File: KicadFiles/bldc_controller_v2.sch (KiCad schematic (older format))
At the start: 175 parts, among them J1 Conn_01x05_Male, J10 Conn_01x02_Female, J11 Conn_01x02_Female, J12 Conn_01x02_Female, J13 Conn_01x02_Female, J14 Conn_01x02_Female, J15 Conn_01x04_Male, J2 Conn_01x03_Male, J3 Conn_01x03_Male, J4 1935174, J5 Conn_01x02_Female, J9 Conn_01x02_Female, Q10 IRLB8721PBF, Q11 IRLB8721PBF, Q2 DMN65D8L-7, Q3 DMN65D8L-7, Q5 IRF4905, Q6 IRLB8721PBF, Q7 IRLB8721PBF, Q8 IRLB8721PBF, Q9 IRLB8721PBF, SW2 D6C40 F1 LFS, SW3 1301.9314, SW4 1301.9314, SW5 SW_Push_DPDT, U1 ATmega328P-PU, U2 uA7810, U3 LM7805_TO220, U4 MCP601-xP, U5 LM339, U6 IRS2004, U7 IRS2004, U8 IRS2004, U9 HCPL-181-00DE, Y1 9B-16.000MBBK-B

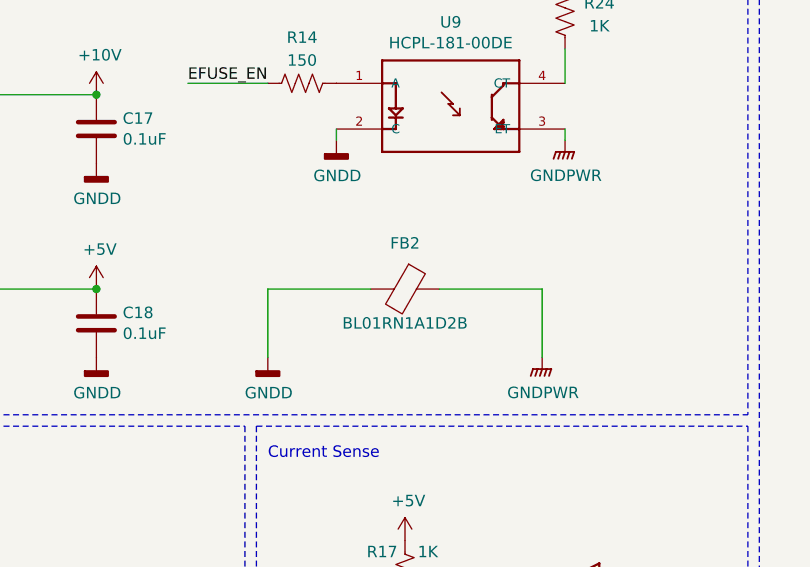
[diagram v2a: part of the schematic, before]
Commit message: Replaced FB with Jumper
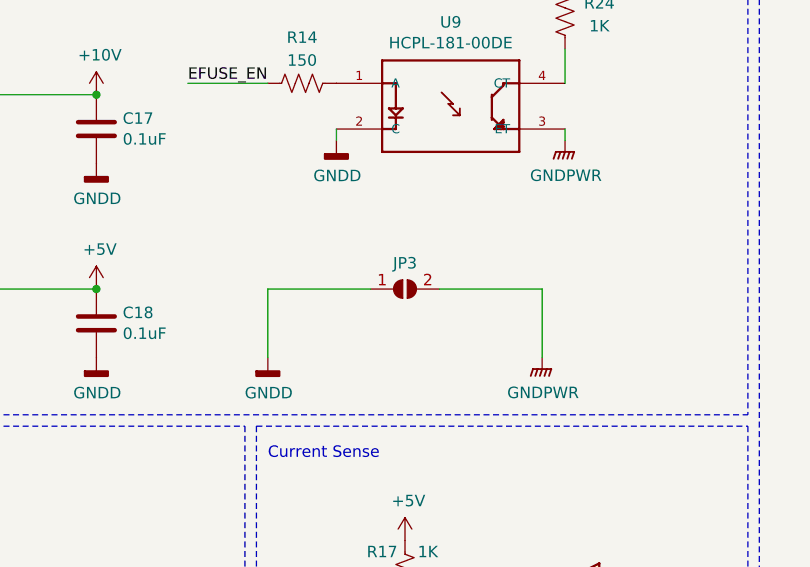
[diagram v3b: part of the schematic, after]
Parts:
- removed FB2: BL01RN1A1D2B, Ferrite_THT:Ferrite_Bead_TH, symbol Device:Ferrite_Bead
- added JP3: SolderJumper_2_Open, Jumper:Solder_Jumper_2_Pin_5A, symbol Jumper:SolderJumper_2_Open
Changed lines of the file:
@@
 Wire Wire Line
 	5500 1900 6000 1900
-$Comp
-L Device:Ferrite_Bead FB2
-U 1 1 5E13E3A5
-P 8400 2750
-F 0 "FB2" V 8200 2750 50  0000 C CNN
-F 1 "BL01RN1A1D2B" V 8550 2750 50  0000 C CNN
-F 2 "Ferrite_THT:Ferrite_Bead_TH" V 8330 2750 50  0001 C CNN
-F 3 "~" H 8400 2750 50  0001 C CNN
-	1    8400 2750
-	0    1    1    0
-$EndComp
 Wire Wire Line
 	8550 2750 9000 2750
@@
 Wire Wire Line
 	2400 1950 2400 2150
+$Comp
+L Jumper:SolderJumper_2_Open JP3
+U 1 1 5EB572A6
+P 8400 2750
+F 0 "JP3" H 8400 2863 50  0000 C CNN
+F 1 "SolderJumper_2_Open" H 8400 2864 50  0001 C CNN
+F 2 "Jumper:Solder_Jumper_2_Pin_5A" H 8400 2750 50  0001 C CNN
+F 3 "~" H 8400 2750 50  0001 C CNN
+	1    8400 2750
+	1    0    0    -1
+$EndComp
 $EndSCHEMATC

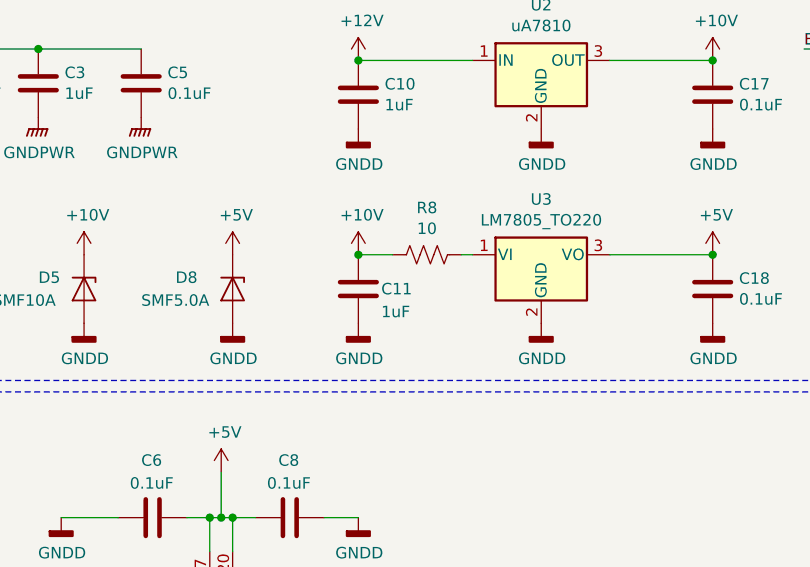
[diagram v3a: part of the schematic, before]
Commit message: Updated 5V Regulator
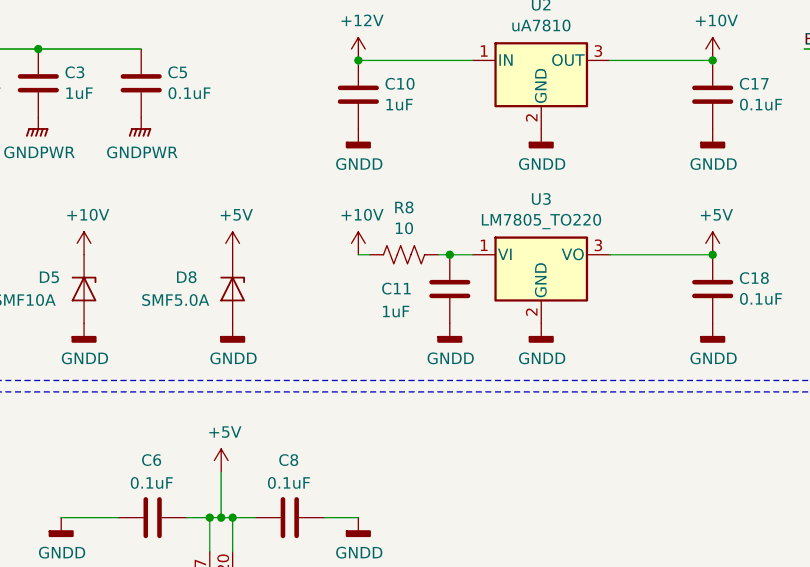
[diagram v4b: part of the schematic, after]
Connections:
- wire segments 325 -> 326
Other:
- moved on the sheet: C11, R8
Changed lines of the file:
@@
 $EndComp
 Wire Wire Line
-	5950 2750 6000 2750
+	5850 2750 5900 2750
 Wire Wire Line
-	5650 2750 5500 2750
+	5550 2750 5500 2750
 $Comp
 L Device:R_US R8
 U 1 1 5DF60A47
-P 5800 2750
-F 0 "R8" V 5595 2750 50  0000 C CNN
-F 1 "10" V 5686 2750 50  0000 C CNN
-F 2 "Resistor_SMD:R_0805_2012Metric_Pad1.15x1.40mm_HandSolder" V 5840 2740 50  0001 C CNN
-F 3 "~" H 5800 2750 50  0001 C CNN
-	1    5800 2750
+P 5700 2750
+F 0 "R8" V 5495 2750 50  0000 C CNN
+F 1 "10" V 5586 2750 50  0000 C CNN
+F 2 "Resistor_SMD:R_0805_2012Metric_Pad1.15x1.40mm_HandSolder" V 5740 2740 50  0001 C CNN
+F 3 "~" H 5700 2750 50  0001 C CNN
+	1    5700 2750
 	0    1    1    0
 $EndComp
@@
 L power:GNDD #PWR052
 U 1 1 5DC455A1
-P 5500 3050
-F 0 "#PWR052" H 5500 2800 50  0001 C CNN
-F 1 "GNDD" H 5504 2895 50  0000 C CNN
-F 2 "" H 5500 3050 50  0001 C CNN
-F 3 "" H 5500 3050 50  0001 C CNN
-	1    5500 3050
+P 5900 3050
+F 0 "#PWR052" H 5900 2800 50  0001 C CNN
+F 1 "GNDD" H 5904 2895 50  0000 C CNN
+F 2 "" H 5900 3050 50  0001 C CNN
+F 3 "" H 5900 3050 50  0001 C CNN
+	1    5900 3050
 	1    0    0    -1
 $EndComp
@@
 $EndComp
 Connection ~ 5500 1900
-Connection ~ 5500 2750
 $Comp
 L power:+5V #PWR013
@@
 L Device:C C11
 U 1 1 5FB5131F
-P 5500 2900
+P 5900 2900
 F 0 "C11" H 5600 2900 50  0000 L CNN
 F 1 "1uF" H 5600 2800 50  0000 L CNN
-F 2 "Capacitor_SMD:C_0805_2012Metric_Pad1.15x1.40mm_HandSolder" H 5538 2750 50  0001 C CNN
-F 3 "~" H 5500 2900 50  0001 C CNN
-	1    5500 2900
+F 2 "Capacitor_SMD:C_0805_2012Metric_Pad1.15x1.40mm_HandSolder" H 5938 2750 50  0001 C CNN
+F 3 "~" H 5900 2900 50  0001 C CNN
+	1    5900 2900
 	1    0    0    -1
 $EndComp
@@
 	1    0    0    -1
 $EndComp
+Connection ~ 5900 2750
+Wire Wire Line
+	5900 2750 6000 2750
 $EndSCHEMATC

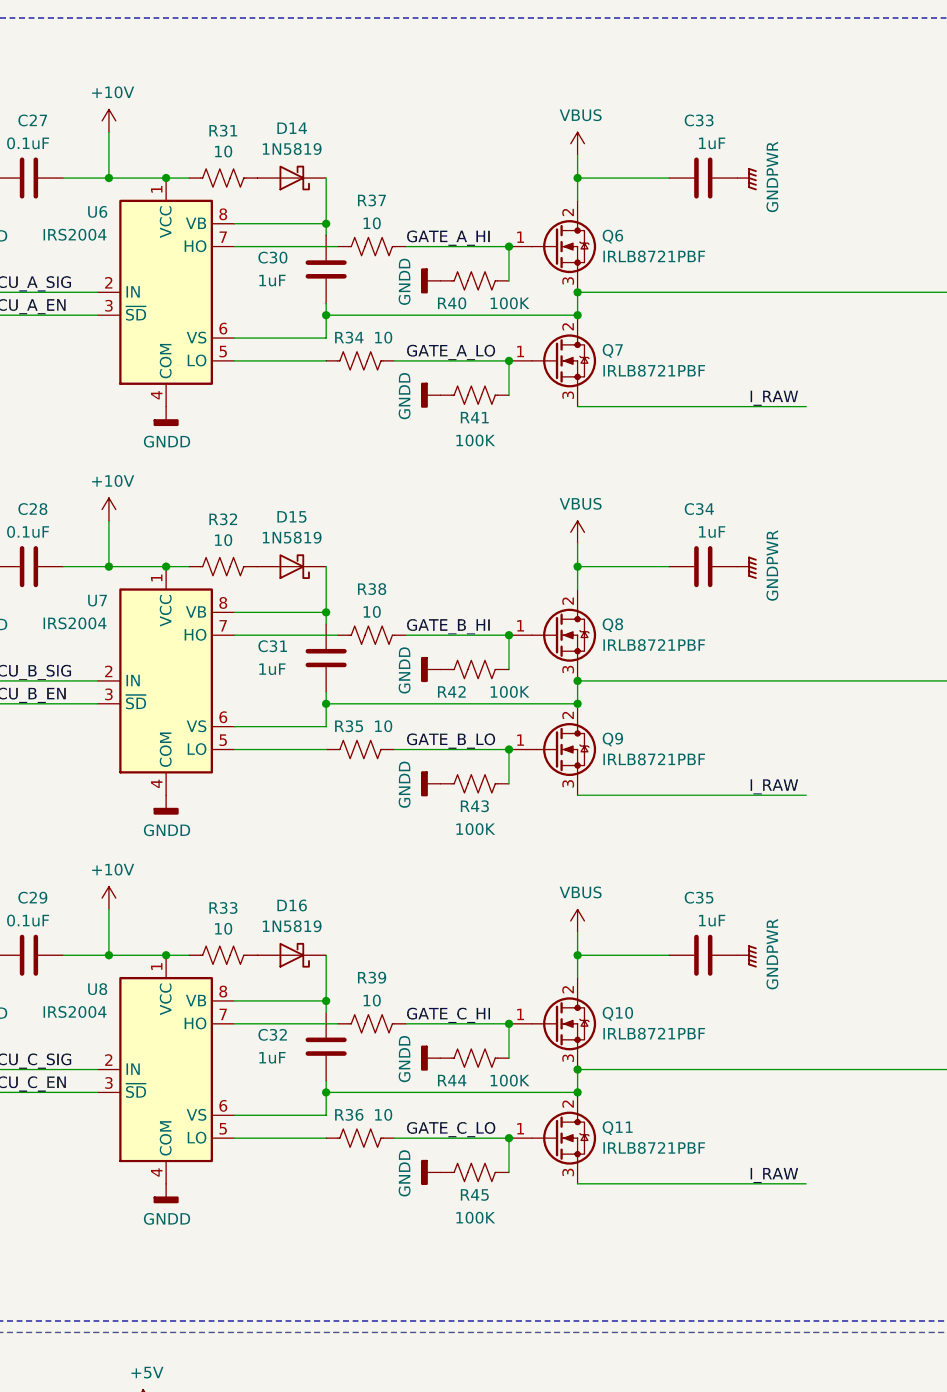
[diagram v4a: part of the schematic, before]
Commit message: Updated FET Placement
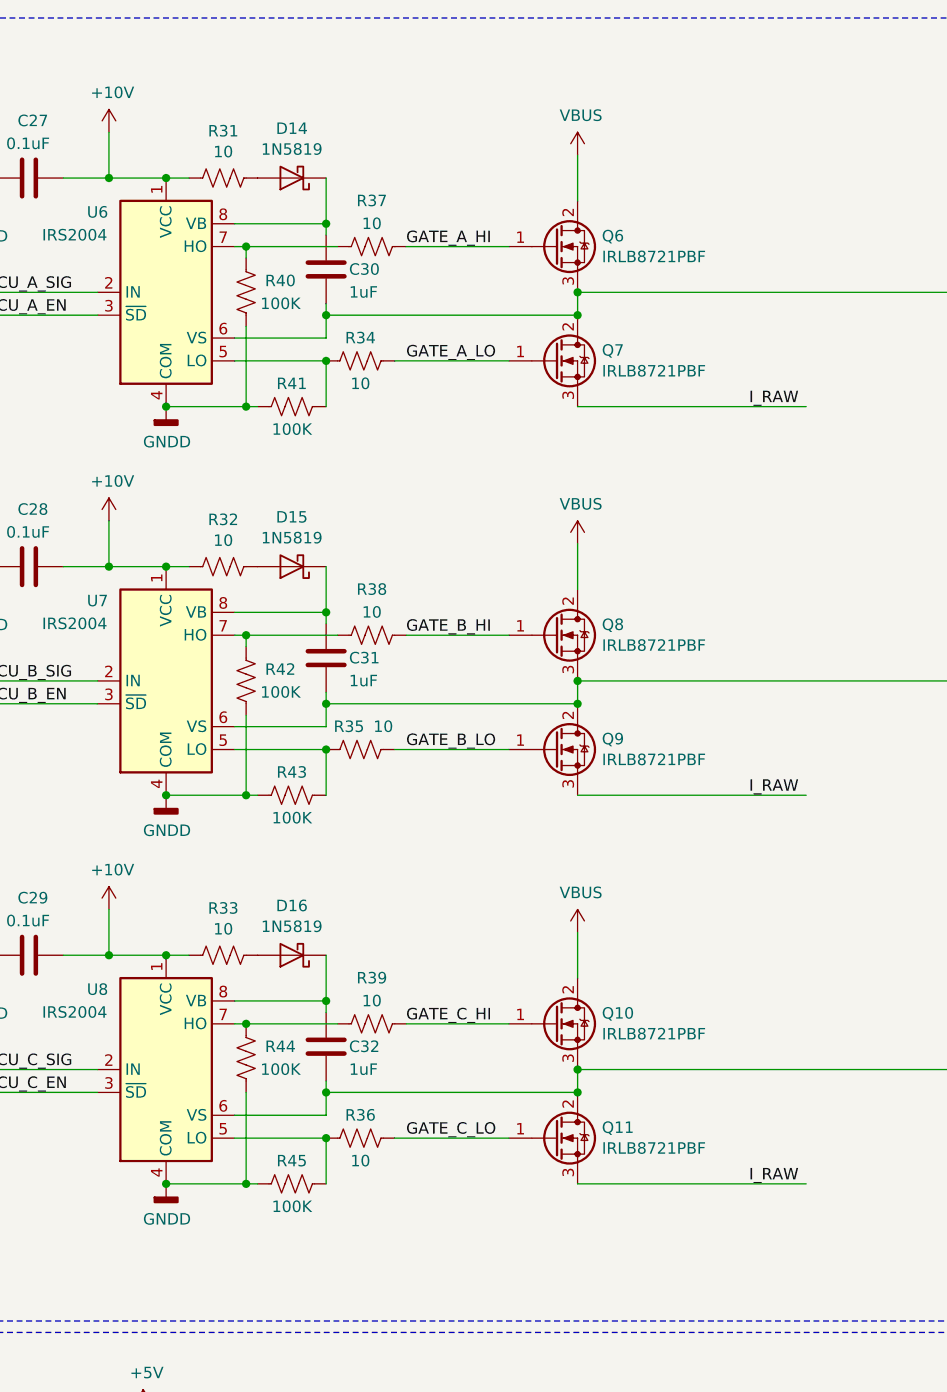
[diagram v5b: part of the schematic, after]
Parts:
- removed C33, C34, C35: 1uF, Capacitor_SMD:C_0805_2012Metric_Pad1.15x1.40mm_HandSolder, symbol Device:C
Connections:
- wire segments 326 -> 331
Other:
- moved on the sheet: R40, R41, R42, R43, R44, R45

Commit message: Ready to Route
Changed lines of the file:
@@
 Text Label 1800 1750 0    50   ~ 0
 EXT_nRST
-Text Label 1800 2050 0    50   ~ 0
-TXD
-Text Label 1800 2150 0    50   ~ 0
-RXD
 $Comp
 L power:+12V #PWR023
@@
 $EndComp
 Wire Wire Line
-	2400 1850 2400 1700
-Wire Wire Line
 	1750 1750 2200 1750
 Wire Wire Line
@@
 Connection ~ 12350 8400
 Wire Wire Line
-	1750 2150 2200 2150
-Wire Wire Line
-	1750 2050 2200 2050
-Wire Wire Line
-	1750 1850 2400 1850
-Wire Wire Line
-	1750 1950 2400 1950
-Wire Wire Line
 	1750 2750 2150 2750
 Text Label 1750 2750 0    50   ~ 0
@@
 Wire Wire Line
 	5450 4650 6050 4650
-Text Label 5600 6250 0    50   ~ 0
+Text Label 5600 6350 0    50   ~ 0
 nI_TRIG
-Text Label 5600 6450 0    50   ~ 0
+Text Label 5600 4750 0    50   ~ 0
 AUX_OUT
-Text Label 5600 5350 0    50   ~ 0
+Text Label 5600 4650 0    50   ~ 0
 EFUSE_EN
 Text Label 5600 5850 0    50   ~ 0
 nRESET
-Text Label 5600 6550 0    50   ~ 0
+Text Label 5600 4850 0    50   ~ 0
 nESTOP
-Text Label 5600 5550 0    50   ~ 0
-I_SENSE
 Text Label 5600 5450 0    50   ~ 0
-ANALOG_IN
-Text Label 5600 5250 0    50   ~ 0
+I_SENSE
+Text Label 5600 4350 0    50   ~ 0
 MCU_A_EN
-Text Label 5600 4850 0    50   ~ 0
+Text Label 5600 6750 0    50   ~ 0
 MCU_B_EN
-Text Label 5600 4750 0    50   ~ 0
+Text Label 5600 6550 0    50   ~ 0
 MCU_C_EN
-Text Label 5600 4650 0    50   ~ 0
+Text Label 5600 4450 0    50   ~ 0
 MCU_A_SIG
 Text Label 5600 4550 0    50   ~ 0
 MCU_B_SIG
-Text Label 5600 4450 0    50   ~ 0
+Text Label 5600 6650 0    50   ~ 0
 MCU_C_SIG
-Text Label 5600 4350 0    50   ~ 0
+Text Label 5600 6450 0    50   ~ 0
 BEMF_B
-Text Label 5600 6650 0    50   ~ 0
+Text Label 5600 5550 0    50   ~ 0
 BEMF_A
-Text Label 5600 6750 0    50   ~ 0
+Text Label 5600 6250 0    50   ~ 0
 BEMF_C
-Text Label 5600 6350 0    50   ~ 0
+Text Label 5600 5350 0    50   ~ 0
 AUX_IN
 Wire Wire Line
@@
 	1    0    0    -1
 $EndComp
-Wire Wire Line
-	2400 1950 2400 2150
 $Comp
 L Jumper:SolderJumper_2_Open JP3
@@
 	11850 5700 11850 5500
 Connection ~ 11850 5500
+Wire Wire Line
+	1750 2050 2200 2050
+Wire Wire Line
+	1750 2150 2200 2150
+Wire Wire Line
+	2400 1850 2400 1700
+Wire Wire Line
+	2400 1950 2400 2150
+Text Label 1800 2150 0    50   ~ 0
+RXD
+Text Label 1800 2050 0    50   ~ 0
+TXD
+Wire Wire Line
+	1750 1950 2400 1950
+Wire Wire Line
+	1750 1850 2400 1850
+Text Label 5600 5250 0    50   ~ 0
+ANALOG_IN
 $EndSCHEMATC

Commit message: Finished Planes
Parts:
- J10, J11, J12, J13, J14, J5, J9: footprint Connector_PinHeader_2.54mm:PinHeader_1x02_P2.54mm_Vertical -> Connector_PinSocket_2.54mm:PinSocket_1x02_P2.54mm_Vertical
- TP18, TP2, TP34, TP4: footprint TestPoint:TestPoint_THTPad_1.0x1.0mm_Drill0.5mm -> TestPoint:TestPoint_Keystone_5000-5004_Miniature
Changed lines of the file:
@@
 F 0 "J14" H 13150 6800 50  0000 C CNN
 F 1 "Conn_01x02_Female" H 14000 6950 50  0001 C CNN
-F 2 "Connector_PinHeader_2.54mm:PinHeader_1x02_P2.54mm_Vertical" H 13250 7000 50  0001 C CNN
+F 2 "Connector_PinSocket_2.54mm:PinSocket_1x02_P2.54mm_Vertical" H 13250 7000 50  0001 C CNN
 F 3 "~" H 13250 7000 50  0001 C CNN
 	1    13250 7000
@@
 F 0 "J11" H 12500 6800 50  0000 C CNN
 F 1 "Conn_01x02_Female" H 13350 6950 50  0001 C CNN
-F 2 "Connector_PinHeader_2.54mm:PinHeader_1x02_P2.54mm_Vertical" H 12600 7000 50  0001 C CNN
+F 2 "Connector_PinSocket_2.54mm:PinSocket_1x02_P2.54mm_Vertical" H 12600 7000 50  0001 C CNN
 F 3 "~" H 12600 7000 50  0001 C CNN
 	1    12600 7000
@@
 F 0 "J12" H 13100 7550 50  0000 C CNN
 F 1 "Conn_01x02_Female" H 13950 7700 50  0001 C CNN
-F 2 "Connector_PinHeader_2.54mm:PinHeader_1x02_P2.54mm_Vertical" H 13200 7750 50  0001 C CNN
+F 2 "Connector_PinSocket_2.54mm:PinSocket_1x02_P2.54mm_Vertical" H 13200 7750 50  0001 C CNN
 F 3 "~" H 13200 7750 50  0001 C CNN
 	1    13200 7750
@@
 F 0 "J9" H 12450 7550 50  0000 C CNN
 F 1 "Conn_01x02_Female" H 13300 7700 50  0001 C CNN
-F 2 "Connector_PinHeader_2.54mm:PinHeader_1x02_P2.54mm_Vertical" H 12550 7750 50  0001 C CNN
+F 2 "Connector_PinSocket_2.54mm:PinSocket_1x02_P2.54mm_Vertical" H 12550 7750 50  0001 C CNN
 F 3 "~" H 12550 7750 50  0001 C CNN
 	1    12550 7750
@@
 F 0 "J13" H 13100 8300 50  0000 C CNN
 F 1 "Conn_01x02_Female" H 13950 8450 50  0001 C CNN
-F 2 "Connector_PinHeader_2.54mm:PinHeader_1x02_P2.54mm_Vertical" H 13200 8500 50  0001 C CNN
+F 2 "Connector_PinSocket_2.54mm:PinSocket_1x02_P2.54mm_Vertical" H 13200 8500 50  0001 C CNN
 F 3 "~" H 13200 8500 50  0001 C CNN
 	1    13200 8500
@@
 F 0 "J10" H 12450 8300 50  0000 C CNN
 F 1 "Conn_01x02_Female" H 13300 8450 50  0001 C CNN
-F 2 "Connector_PinHeader_2.54mm:PinHeader_1x02_P2.54mm_Vertical" H 12550 8500 50  0001 C CNN
+F 2 "Connector_PinSocket_2.54mm:PinSocket_1x02_P2.54mm_Vertical" H 12550 8500 50  0001 C CNN
 F 3 "~" H 12550 8500 50  0001 C CNN
 	1    12550 8500
@@
 F 0 "J5" H 8200 4300 50  0000 C CNN
 F 1 "Conn_01x02_Female" H 8850 4300 50  0001 C CNN
-F 2 "Connector_PinHeader_2.54mm:PinHeader_1x02_P2.54mm_Vertical" H 8100 4350 50  0001 C CNN
+F 2 "Connector_PinSocket_2.54mm:PinSocket_1x02_P2.54mm_Vertical" H 8100 4350 50  0001 C CNN
 F 3 "~" H 8100 4350 50  0001 C CNN
 	1    8100 4350
@@
 F 0 "TP4" H 1750 5650 50  0000 R CNN
 F 1 "TestPoint" H 1592 5517 50  0001 R CNN
-F 2 "TestPoint:TestPoint_THTPad_1.0x1.0mm_Drill0.5mm" H 1850 5400 50  0001 C CNN
+F 2 "TestPoint:TestPoint_Keystone_5000-5004_Miniature" H 1850 5400 50  0001 C CNN
 F 3 "~" H 1850 5400 50  0001 C CNN
 	1    1650 5400
@@
 F 0 "TP2" H 1250 5650 50  0000 R CNN
 F 1 "TestPoint" H 1092 5517 50  0001 R CNN
-F 2 "TestPoint:TestPoint_THTPad_1.0x1.0mm_Drill0.5mm" H 1350 5400 50  0001 C CNN
+F 2 "TestPoint:TestPoint_Keystone_5000-5004_Miniature" H 1350 5400 50  0001 C CNN
 F 3 "~" H 1350 5400 50  0001 C CNN
 	1    1150 5400
@@
 F 0 "TP34" H 2750 5650 50  0000 R CNN
 F 1 "TestPoint" H 2592 5517 50  0001 R CNN
-F 2 "TestPoint:TestPoint_THTPad_1.0x1.0mm_Drill0.5mm" H 2850 5400 50  0001 C CNN
+F 2 "TestPoint:TestPoint_Keystone_5000-5004_Miniature" H 2850 5400 50  0001 C CNN
 F 3 "~" H 2850 5400 50  0001 C CNN
 	1    2650 5400
@@
 F 0 "TP18" H 2250 5650 50  0000 R CNN
 F 1 "TestPoint" H 2092 5517 50  0001 R CNN
-F 2 "TestPoint:TestPoint_THTPad_1.0x1.0mm_Drill0.5mm" H 2350 5400 50  0001 C CNN
+F 2 "TestPoint:TestPoint_Keystone_5000-5004_Miniature" H 2350 5400 50  0001 C CNN
 F 3 "~" H 2350 5400 50  0001 C CNN
 	1    2150 5400

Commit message: Finished First Pass of Routing
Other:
- moved on the sheet: SW2
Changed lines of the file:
@@
 F 3 "~" H 6250 9750 50  0001 C CNN
 	1    6250 9550
-	1    0    0    -1
+	-1   0    0    1
 $EndComp
 $Comp
@@
 	6650 9250 6950 9250
 Connection ~ 6950 9250
-Text Notes 6150 9700 0    50   ~ 10
+Text Notes 6150 9500 0    50   ~ 10
 ESTOP
 $Comp
@@
 Wire Wire Line
 	2150 4050 1750 4050
+Text Label 1750 4050 0    50   ~ 0
+I2C_SDA
 Text Label 1750 4150 0    50   ~ 0
-I2C_SDA
-Text Label 1750 4050 0    50   ~ 0
 I2C_SCL
 $Comp
